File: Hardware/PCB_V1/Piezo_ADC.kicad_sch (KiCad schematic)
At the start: 51 parts, among them J1 Conn_RJ45_Shielded_8p8c_RA_A-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, J2 Conn_2Pos_3.96mm_1Row_TH_JST_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, U1 IC_LDO_FIXED_3.3V_SC-70-5, U2 IC_TRANSCIEVER_RS485_DUPLEX_S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, U3 IC_ADC_SPI_12BIT_ADC121S021_S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, U4 IC_OPAMP_1MHz_TLV9001IDBVR_1A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, U5 IC_TRANSCIEVER_RS485_DUPLEX_S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

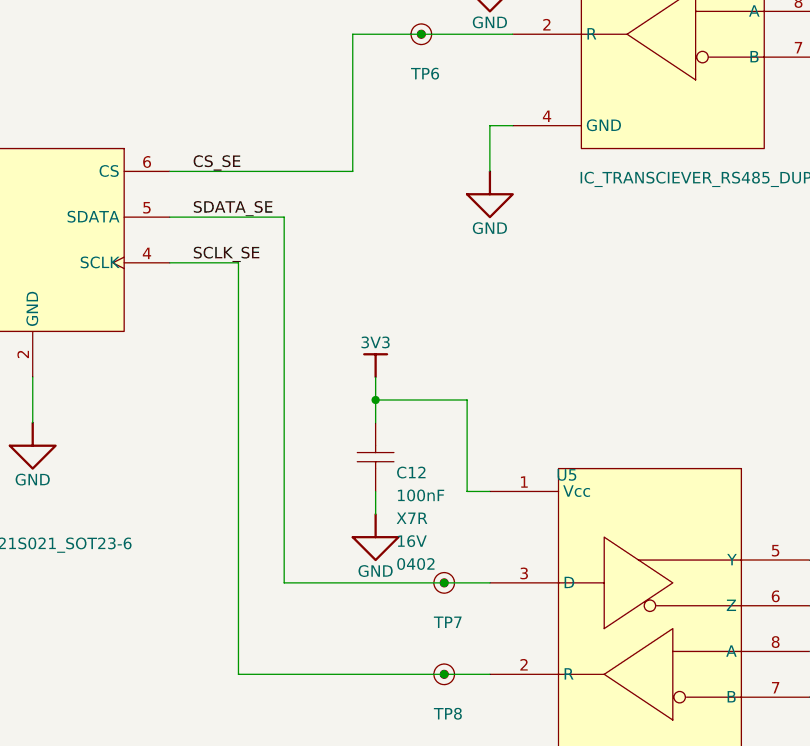
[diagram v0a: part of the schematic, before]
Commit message: Converted Altium PCB File to KiCAD
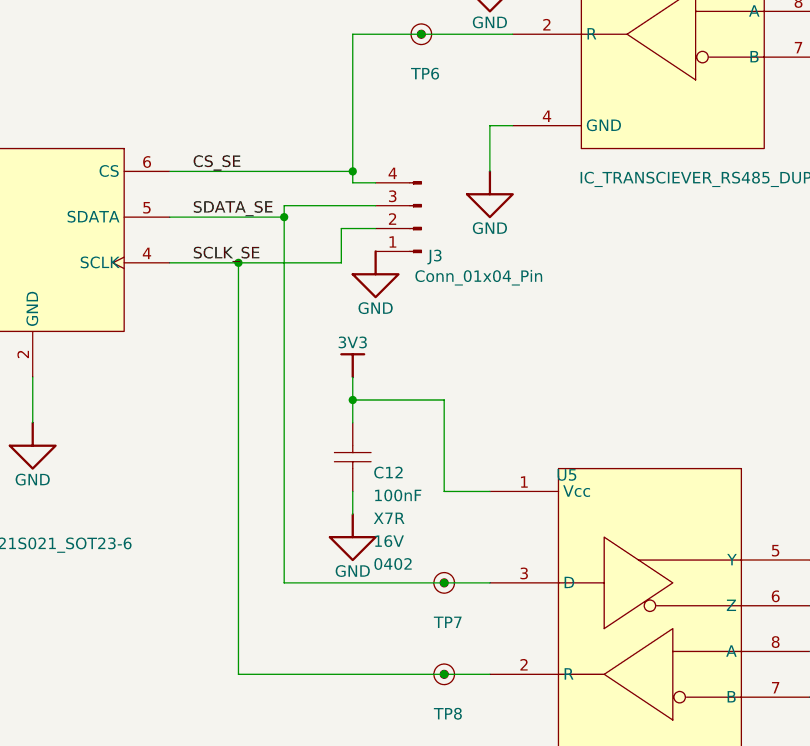
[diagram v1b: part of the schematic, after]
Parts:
- added J3: Conn_01x04_Pin, Connector_PinHeader_2.54mm:PinHeader_1x04_P2.54mm_Vertical, symbol Connector:Conn_01x04_Pin
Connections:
- net CS_SE: now also J3.4 (Pin_4)
- net GND: now also J3.1 (Pin_1)
- net SCLK_SE: now also J3.2 (Pin_2)
- net SDATA_SE: now also J3.3 (Pin_3)
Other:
- moved on the sheet: C12

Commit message: Added 5015 test points to schematic
Waiting to get confirmation before I place them on the board.
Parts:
- removed J3: Conn_01x04_Pin, Connector_PinHeader_2.54mm:PinHeader_1x04_P2.54mm_Vertical, symbol Connector:Conn_01x04_Pin
- TP6, TP7, TP8: footprint TP06R -> TestPoint:TestPoint_Keystone_5015_Micro_Mini
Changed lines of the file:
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@@
 	)
 	(junction
-		(at 279.4 144.78)
-		(diameter 0)
-		(color 0 0 0 0)
-	)
-	(junction
 		(at 99.06 22.86)
 		(diameter 0)
@@
 	)
 	(junction
-		(at 271.78 149.86)
-		(diameter 0)
-		(color 0 0 0 0)
-	)
-	(junction
 		(at 208.28 127)
 		(diameter 0)
@@
 	)
 	(junction
-		(at 266.7 154.94)
-		(diameter 0)
-		(color 0 0 0 0)
-	)
-	(junction
 		(at 139.7 129.54)
 		(diameter 0)
@@
 	(wire
 		(pts
-			(xy 278.13 154.94) (xy 278.13 151.13)
-		)
-		(stroke
-			(width 0)
-			(type default)
-		)
-	)
-	(wire
-		(pts
 			(xy 20.32 53.34) (xy 20.32 48.26)
 		)
@@
 	(wire
 		(pts
-			(xy 279.4 144.78) (xy 279.4 146.05)
-		)
-		(stroke
-			(width 0)
-			(type default)
-		)
-	)
-	(wire
-		(pts
 			(xy 68.58 175.26) (xy 68.58 180.34)
 		)
@@
 	(wire
 		(pts
-			(xy 271.78 148.59) (xy 271.78 149.86)
-		)
-		(stroke
-			(width 0)
-			(type default)
-		)
-	)
-	(wire
-		(pts
 			(xy 111.76 177.8) (xy 111.76 172.72)
 		)
@@
 	(wire
 		(pts
-			(xy 266.7 154.94) (xy 278.13 154.94)
-		)
-		(stroke
-			(width 0)
-			(type default)
-		)
-	)
-	(wire
-		(pts
 			(xy 68.58 157.48) (xy 73.66 157.48)
 		)
@@
 		)
 	)
-	(wire
-		(pts
-			(xy 271.78 148.59) (xy 281.94 148.59)
-		)
-		(stroke
-			(width 0)
-			(type default)
-		)
-	)
 	(polyline
 		(pts
@@
 	(wire
 		(pts
-			(xy 279.4 146.05) (xy 281.94 146.05)
-		)
-		(stroke
-			(width 0)
-			(type default)
-		)
-	)
-	(wire
-		(pts
 			(xy 266.7 200.66) (xy 266.7 154.94)
 		)
@@
 		)
 	)
-	(wire
-		(pts
-			(xy 278.13 151.13) (xy 281.94 151.13)
-		)
-		(stroke
-			(width 0)
-			(type default)
-		)
-	)
 	(polyline
 		(pts
@@
 	)
 	(symbol
-		(lib_id "Connector:Conn_01x04_Pin")
-		(at 287.02 151.13 180)
-		(unit 1)
-		(body_style 1)
-		(exclude_from_sim no)
-		(in_bom yes)
-		(on_board yes)
-		(in_pos_files yes)
-		(dnp no)
-		(property "Reference" "J3"
-			(at 287.782 154.178 0)
-			(show_name no)
-			(do_not_autoplace no)
-			(effects
-				(font
-					(size 1.27 1.27)
-				)
-				(justify right)
-			)
-		)
-		(property "Value" "Conn_01x04_Pin"
-			(at 286.258 156.464 0)
-			(show_name no)
-			(do_not_autoplace no)
-			(effects
-				(font
-					(size 1.27 1.27)
-				)
-				(justify right)
-			)
-		)
-		(property "Footprint" "Connector_PinHeader_2.54mm:PinHeader_1x04_P2.54mm_Vertical"
-			(at 287.02 151.13 0)
-			(hide yes)
-			(show_name no)
-			(do_not_autoplace no)
-			(effects
-				(font
-					(size 1.27 1.27)
-				)
-			)
-		)
-		(property "Datasheet" ""
-			(at 287.02 151.13 0)
-			(hide yes)
-			(show_name no)
-			(do_not_autoplace no)
-			(effects
-				(font
-					(size 1.27 1.27)
-				)
-			)
-		)
-		(property "Description" "Generic connector, single row, 01x04, script generated"
-			(at 287.02 151.13 0)
-			(hide yes)
-			(show_name no)
-			(do_not_autoplace no)
-			(effects
-				(font
-					(size 1.27 1.27)
-				)
-			)
-		)
-		(pin "2"
-		)
-		(pin "1"
-		)
-		(pin "3"
-		)
-		(pin "4"
-		)
-		(instances
-			(project "Piezo_ADC"
-				(path "/b59525dd-c3a5-42c4-90f7-d761f18c34ae"
-					(reference "J3")
-					(unit 1)
-				)
-			)
-		)
-	)
-	(symbol
 		(lib_id "Maven Robotics:root_0_CMP-001-0001-4_Maven Robotics")
 		(at 289.56 200.66 90)
@@
 			)
 		)
-		(property "Footprint" "TP06R"
+		(property "Footprint" "TestPoint:TestPoint_Keystone_5015_Micro_Mini"
 			(at 289.56 200.66 0)
 			(hide yes)
@@
 			)
 		)
-		(property "Footprint" "TP06R"
+		(property "Footprint" "TestPoint:TestPoint_Keystone_5015_Micro_Mini"
 			(at 289.56 190.5 0)
 			(hide yes)
@@
 			)
 		)
-		(property "Footprint" "TP06R"
+		(property "Footprint" "TestPoint:TestPoint_Keystone_5015_Micro_Mini"
 			(at 287.02 129.54 0)
 			(hide yes)
@@
 					(unit 1)
 				)
-			)
-		)
-	)
-	(symbol
-		(lib_id "Piezo_ADC-altium-import:GND_SIGNAL_GROUND")
-		(at 281.94 153.67 0)
-		(unit 1)
-		(body_style 1)
-		(exclude_from_sim no)
-		(in_bom yes)
-		(on_board yes)
-		(in_pos_files yes)
-		(dnp no)
-		(property "Reference" "#PWR01"
-			(at 281.94 153.67 0)
-			(hide yes)
-			(show_name no)
-			(do_not_autoplace no)
-			(effects
-				(font
-					(size 1.27 1.27)
-				)
-			)
-		)
-		(property "Value" "GND"
-			(at 281.94 160.02 0)
-			(show_name no)
-			(do_not_autoplace no)
-			(effects
-				(font
-					(size 1.27 1.27)
-				)
-			)
-		)
-		(property "Footprint" ""
-			(at 281.94 153.67 0)
-			(show_name no)
-			(do_not_autoplace no)
-			(effects
-				(font
-					(size 1.27 1.27)
-				)
-			)
-		)
-		(property "Datasheet" ""
-			(at 281.94 153.67 0)
-			(show_name no)
-			(do_not_autoplace no)
-			(effects
-				(font
-					(size 1.27 1.27)
-				)
-			)
-		)
-		(property "Description" ""
-			(at 281.94 153.67 0)
-			(show_name no)
-			(do_not_autoplace no)
-			(effects
-				(font
-					(size 1.27 1.27)
-				)
-			)
-		)
-		(pin ""
-		)
-		(instances
-			(project "Piezo_ADC"
-				(path "/b59525dd-c3a5-42c4-90f7-d761f18c34ae"
-					(reference "#PWR01")
-					(unit 1)
-				)

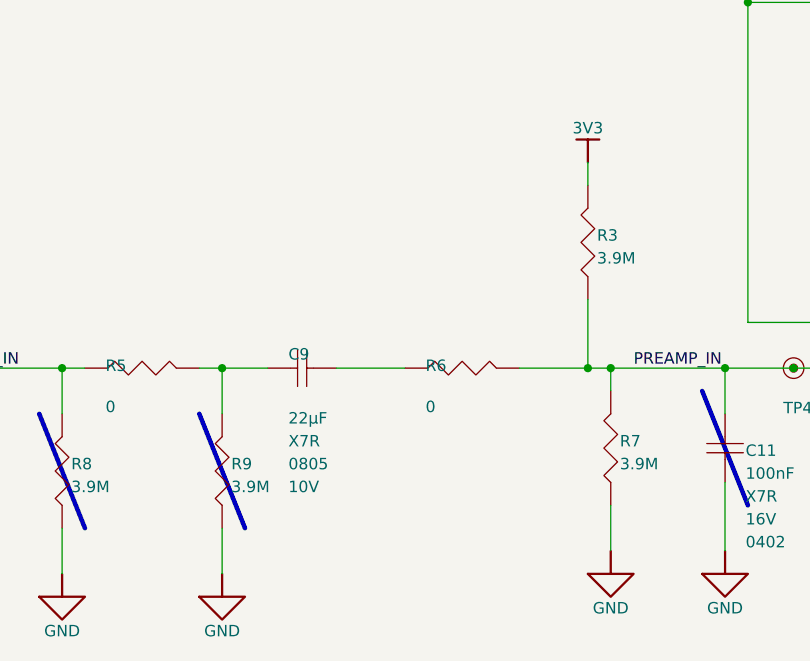
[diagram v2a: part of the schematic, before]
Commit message: Added Schottky Diodes
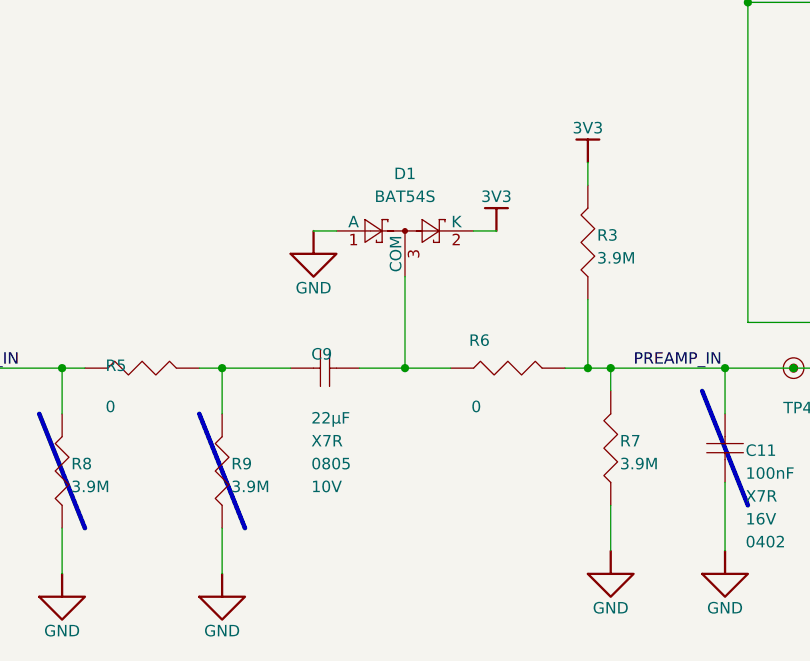
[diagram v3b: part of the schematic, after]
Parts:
- added D1: BAT54S, Package_TO_SOT_SMD:SOT-23, symbol Diode:BAT54S
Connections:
- net 3V3: now also D1.2 (K)
- net GND: now also D1.1 (A)
- net at C9.2, R6.1: now also D1.3 (COM)
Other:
- moved on the sheet: C9, R6

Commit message: PCB Updates
- Added keystone 5001 test points
- Added Schottky diodes
- reworked the board layout to make room for TPs and additional components.
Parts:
- added C13: Cap_1nF_10%_16V_0402, Piezo_Footprints:CAP_0402_0.6mm_Height, symbol Maven Robotics:root_3_CAP-NP-2_Maven Robotics
- added R13, R14: Res_2.26kR0_1%_63mW_0402, Piezo_Footprints:RES_0402, symbol Maven Robotics:root_0_RES-2_Maven Robotics_0
- added R15: Res_0R0_1%_63mW_0402, Piezo_Footprints:RES_0402, symbol Maven Robotics:root_0_RES-2_Maven Robotics_0
- C1, C2, C3, C6, C7: footprint CAP_0402_0.6mm_Height -> Piezo_Footprints:CAP_0402_0.6mm_Height
- C10, C12, C4, C5, C8: footprint CAP_0402_0.6mm_Height -> Piezo_Footprints:CAP_0402_0.6mm_Height; ALTIUM_VALUE 100nF -> 0.1uF
- C11: value Cap_0.1uF_10%_16V_0402 -> Cap_2.05nF_10%_16V_0402; footprint CAP_0402_0.6mm_Height -> Piezo_Footprints:CAP_0402_0.6mm_Height; ALTIUM_VALUE 100nF -> 2.05nF
- C9: footprint CAP_0805_1.45mm_Height -> Piezo_Footprints:CAP_0805_1.45mm_Height
- DS1, DS2: footprint LED_0402_Green_KA -> Piezo_Footprints:LED_0402_Green_KA
- FD1, FD2, FD3, FD4, FD5, FD6: footprint FID1X2R -> Piezo_Footprints:FID1X2R
- J1: footprint A-2004-2-4-LPS-N-R -> Piezo_Footprints:A-2004-2-4-LPS-N-R
- J2: footprint JST_B2PS-VH-FP -> Piezo_Footprints:JST_B2PS-VH-FP
- MP1, MP2, MP3, MP4: footprint 9774020960 -> Piezo_Footprints:9774020960
- R1, R10, R11, R12, R2, R3, R4, R5, R6, R7, R8, R9: footprint RES_0402 -> Piezo_Footprints:RES_0402
- TP1, TP3, TP5: footprint TP06R -> Piezo_Footprints:Keystone 5001 TP
- TP2, TP4: footprint TP06R -> Piezo_Footprints:TP06R
- TP6, TP7, TP8: footprint TestPoint:TestPoint_Keystone_5015_Micro_Mini -> Piezo_Footprints:Keystone 5001 TP
- U1, U4: footprint SOT23-5 -> Piezo_Footprints:SOT23-5
- U2, U5: footprint SOIC-8 -> Piezo_Footprints:SOIC-8
- U3: footprint SOT-23-6 -> Piezo_Footprints:SOT-23-6
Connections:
- net GND: now also C13.2
- net PIEZO_IN: now also R15.1; no longer R5.1, R8.2
- net PREAMP_IN: now also C13.1, R14.2; no longer C11.1, R3.1, R6.2, R7.2
- new net: R13.1, R3.1, R6.2, R7.2
- new net: C11.1, R13.2, R14.1
- new net: R15.2, R5.1, R8.2
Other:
- moved on the sheet: C1, C10, C11, C2, C3, C4, C9, D1, DS1, DS2, J2, R1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
